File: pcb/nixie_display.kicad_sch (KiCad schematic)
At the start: 12 parts, among them U1 IC_HV5622PG-G, U2 IC_HV5622PG-G

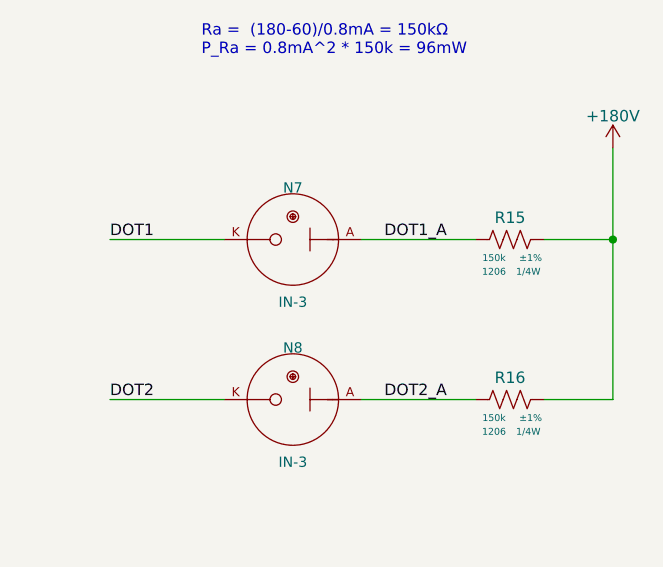
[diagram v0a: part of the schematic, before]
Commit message: Added snubber DNP footprints and named nets on power page.
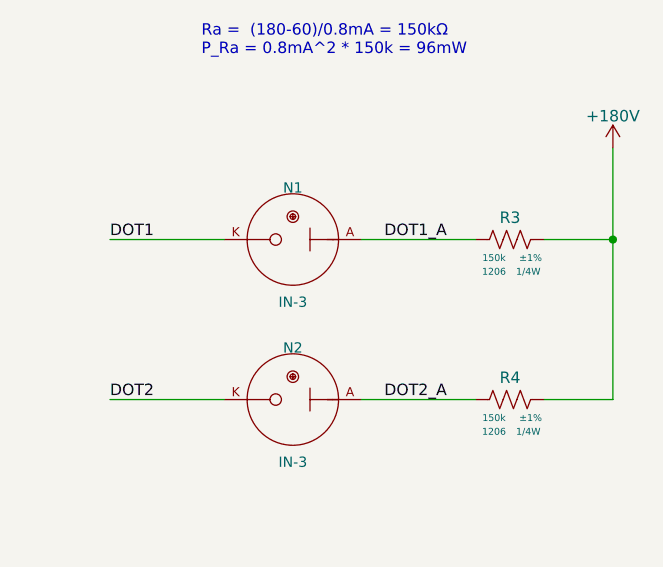
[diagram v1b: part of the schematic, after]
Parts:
- renumbered N7 to N1, N8 to N2, R15 to R3, R16 to R4
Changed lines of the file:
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@@
   (symbol (lib_id "arjun_symbols:RES_150K_1P_1{slash}4W_1206") (at 368.3 124.46 270) (unit 1)
     (in_bom yes) (on_board yes)
-    (property "Reference" "R15" (id 0) (at 364.49 121.285 90)
+    (property "Reference" "R3" (id 0) (at 364.49 121.285 90)
       (effects (font (size 1.27 1.27)) (justify top))
     )
@@
   (symbol (lib_id "arjun_symbols:RES_150K_1P_1{slash}4W_1206") (at 368.3 142.24 270) (unit 1)
     (in_bom yes) (on_board yes)
-    (property "Reference" "R16" (id 0) (at 364.49 139.065 90)
+    (property "Reference" "R4" (id 0) (at 364.49 139.065 90)
       (effects (font (size 1.27 1.27)) (justify top))
     )
@@
   (symbol (lib_id "arjun_symbols:+180V") (at 375.92 114.3 0) (unit 1)
     (in_bom yes) (on_board yes)
-    (property "Reference" "#PWR042" (id 0) (at 375.92 118.11 0)
+    (property "Reference" "#PWR07" (id 0) (at 375.92 118.11 0)
       (effects (font (size 1.27 1.27)) hide)
     )
@@
   (symbol (lib_id "arjun_symbols:IN-3") (at 347.98 142.24 0) (mirror y) (unit 1)
     (in_bom yes) (on_board yes)
-    (property "Reference" "N8" (id 0) (at 340.36 137.16 0)
+    (property "Reference" "N2" (id 0) (at 340.36 137.16 0)
       (effects (font (size 1.143 1.143)) (justify bottom))
     )
@@
   (symbol (lib_id "arjun_symbols:IN-3") (at 347.98 124.46 0) (mirror y) (unit 1)
     (in_bom yes) (on_board yes)
-    (property "Reference" "N7" (id 0) (at 340.36 119.38 0)
+    (property "Reference" "N1" (id 0) (at 340.36 119.38 0)
       (effects (font (size 1.143 1.143)) (justify bottom))
     )

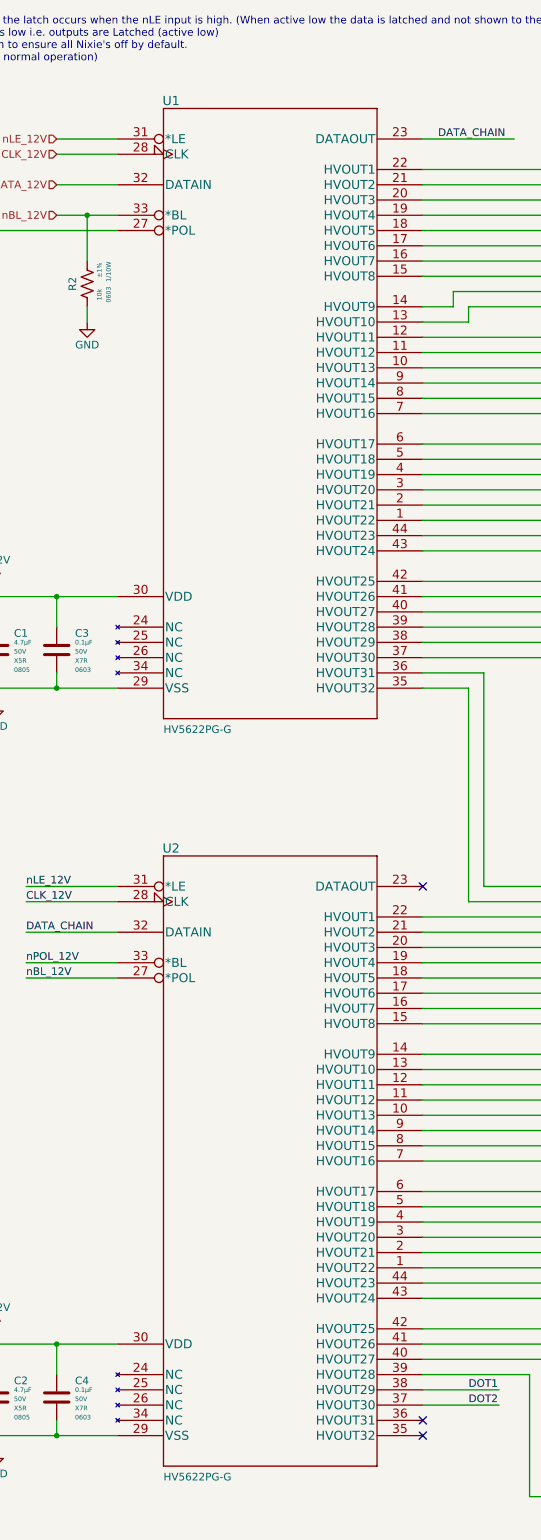
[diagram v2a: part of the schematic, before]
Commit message: Added load switch to input to limit inrush
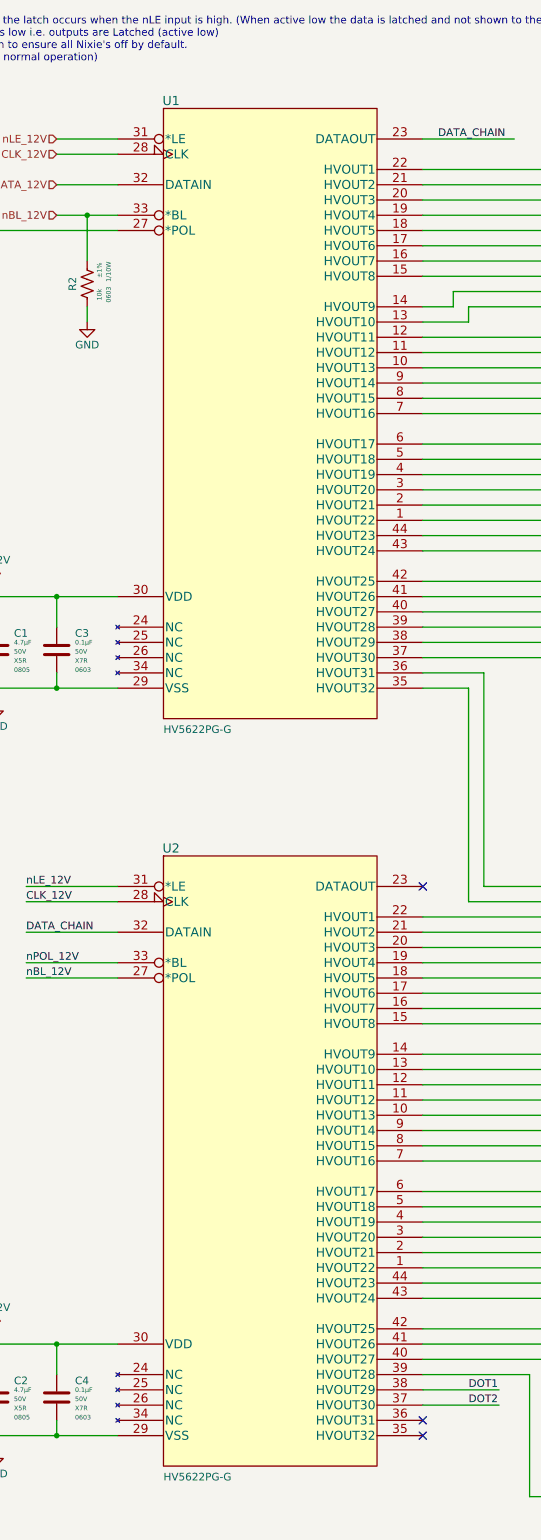
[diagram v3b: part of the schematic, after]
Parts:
- removed U1, U2: IC_HV5622PG-G, arjun_footprints:HV5622PG-G, symbol arjun_symbols:IC_SR_HV5622PG-G
- added U1, U2: IC_SR_MC_HV5622PG-G, arjun_footprints:HV5622PG-G, symbol .arjun:IC_SR_MC_HV5622PG-G
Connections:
- net +12V: now also U1.30 (VDD), U2.30 (VDD)
- net CLK_12V: now also U1.28 (CLK), U2.28 (CLK)
- net DATA_12V: now also U1.32 (DATAIN)
- net DATA_CHAIN: now also U1.23 (DATAOUT), U2.32 (DATAIN)
- net DOT1: now also U2.38 (HVOUT29)
- net DOT2: now also U2.37 (HVOUT30)
- net GND: now also U1.29 (VSS), U2.29 (VSS)
- net H1_0: now also U1.22 (HVOUT1)
- net H1_1: now also U1.21 (HVOUT2)
- net H1_2: now also U1.20 (HVOUT3)
- net H1_3: now also U1.19 (HVOUT4)
- net H1_4: now also U1.18 (HVOUT5)
- net H1_5: now also U1.17 (HVOUT6)
- net H1_6: now also U1.16 (HVOUT7)
- net H1_7: now also U1.15 (HVOUT8)
- net H1_8: now also U1.14 (HVOUT9)
- net H1_9: now also U1.13 (HVOUT10)
- net H2_0: now also U1.12 (HVOUT11)
- net H2_1: now also U1.11 (HVOUT12)
- net H2_2: now also U1.10 (HVOUT13)
- net H2_3: now also U1.9 (HVOUT14)
- net H2_4: now also U1.8 (HVOUT15)
- net H2_5: now also U1.7 (HVOUT16)
- net H2_6: now also U1.6 (HVOUT17)
- net H2_7: now also U1.5 (HVOUT18)
- net H2_8: now also U1.4 (HVOUT19)
- net H2_9: now also U1.3 (HVOUT20)
- net M1_0: now also U1.2 (HVOUT21)
- net M1_1: now also U1.1 (HVOUT22)
- net M1_2: now also U1.44 (HVOUT23)
- net M1_3: now also U1.43 (HVOUT24)
- net M1_4: now also U1.42 (HVOUT25)
- net M1_5: now also U1.41 (HVOUT26)
- net M1_6: now also U1.40 (HVOUT27)
- net M1_7: now also U1.39 (HVOUT28)
- net M1_8: now also U1.38 (HVOUT29)
- net M1_9: now also U1.37 (HVOUT30)
- net M2_0: now also U1.36 (HVOUT31)
- net M2_1: now also U1.35 (HVOUT32)
- net M2_2: now also U2.22 (HVOUT1)
- net M2_3: now also U2.21 (HVOUT2)
- net M2_4: now also U2.20 (HVOUT3)
- net M2_5: now also U2.19 (HVOUT4)
- net M2_6: now also U2.18 (HVOUT5)
- net M2_7: now also U2.17 (HVOUT6)
- net M2_8: now also U2.16 (HVOUT7)
- net M2_9: now also U2.15 (HVOUT8)
- net S1_0: now also U2.14 (HVOUT9)
- net S1_1: now also U2.13 (HVOUT10)
- net S1_2: now also U2.12 (HVOUT11)
- net S1_3: now also U2.11 (HVOUT12)
- net S1_4: now also U2.10 (HVOUT13)
- net S1_5: now also U2.9 (HVOUT14)
- net S1_6: now also U2.8 (HVOUT15)
- net S1_7: now also U2.7 (HVOUT16)
- net S1_8: now also U2.6 (HVOUT17)
- net S1_9: now also U2.5 (HVOUT18)
- net S2_0: now also U2.4 (HVOUT19)
- net S2_1: now also U2.3 (HVOUT20)
- net S2_2: now also U2.2 (HVOUT21)
- net S2_3: now also U2.1 (HVOUT22)
- net S2_4: now also U2.44 (HVOUT23)
- net S2_5: now also U2.43 (HVOUT24)
- net S2_6: now also U2.42 (HVOUT25)
- net S2_7: now also U2.41 (HVOUT26)
- net S2_8: now also U2.40 (HVOUT27)
- net S2_9: now also U2.39 (HVOUT28)
- net nBL_12V: now also U1.33 (*BL), U2.27 (*POL)
- net nLE_12V: now also U1.31 (*LE), U2.31 (*LE)
- net nPOL_12V: now also U1.27 (*POL), U2.33 (*BL)

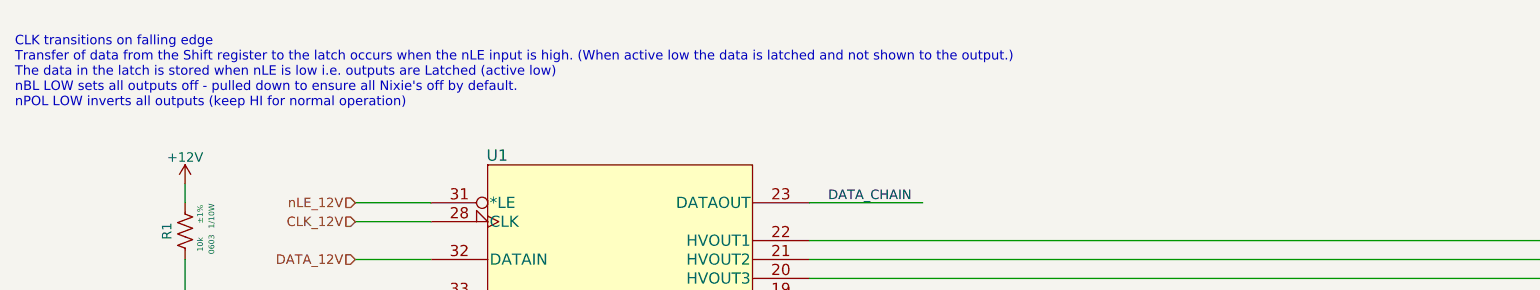
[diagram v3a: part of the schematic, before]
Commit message: Added ESD protection to 5V input, leds, hw rev pins, and test points.
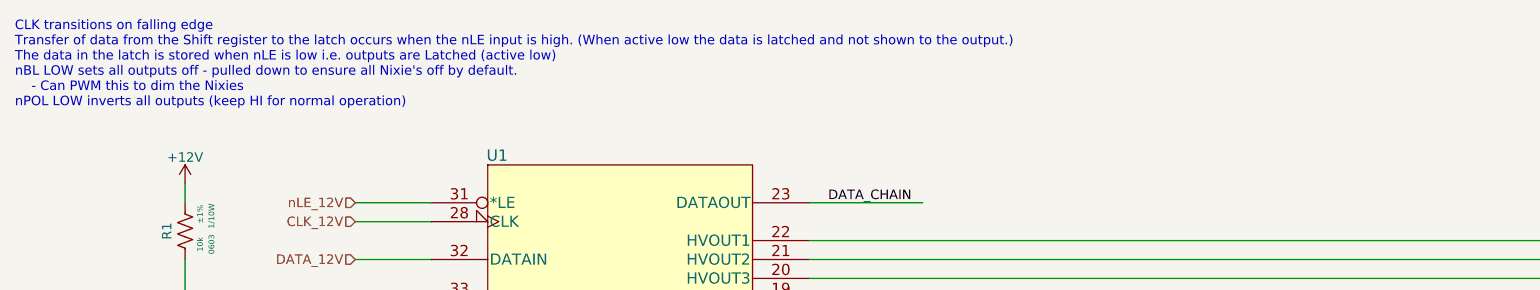
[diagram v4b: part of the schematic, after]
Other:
- note added: "CLK transitions on falling edge Transfer of data from the Shift register to the latch occurs when the nLE input is high. (When active low the data is latched and not shown to the output.) The data in the latch is stored when nLE is low i.e. outputs are Latched (active low) nBL LOW sets all outputs off - pulled down to ensure all Nixie's off by default. - Can PWM this to dim the Nixies nPOL LOW in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"
- note removed: "CLK transitions on falling edge Transfer of data from the Shift register to the latch occurs when the nLE input is high. (When active low the data is latched and not shown to the output.) The data in the latch is stored when nLE is low i.e. outputs are Latched (active low) nBL LOW sets all outputs off - pulled down to ensure all Nixie's off by default. nPOL LOW inverts all outputs (keep HI for no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"
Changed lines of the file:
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@@
     (stroke (width 0) (type default) (color 0 0 0 0))
   )
-  (text "CLK transitions on falling edge\nTransfer of data from the Shift register to the latch occurs when the nLE input is high. (When active low the data is latched and not shown to the output.)\nThe data in the latch is stored when nLE is low i.e. outputs are Latched (active low)\nnBL LOW sets all outputs off - pulled down to ensure all Nixie's off by default.\nnPOL LOW inverts all outputs (keep HI for normal operation)\n"
+  (text "CLK transitions on falling edge\nTransfer of data from the Shift register to the latch occurs when the nLE input is high. (When active low the data is latched and not shown to the output.)\nThe data in the latch is stored when nLE is low i.e. outputs are Latched (active low)\nnBL LOW sets all outputs off - pulled down to ensure all Nixie's off by default.\n	- Can PWM this to dim the Nixies\nnPOL LOW inverts all outputs (keep HI for normal operation)\n"
     (at 15.24 25.4 0)
     (effects (font (size 1.27 1.27)) (justify left bottom))

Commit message: Started layout!! 180V boost mostly laid out
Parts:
- R1, R2: symbol arjun_symbols:RES_10K_1P_1/10W_0603 -> arjun_symbols:RES_10K_1P_1/10W_0603
- R3, R4: symbol arjun_symbols:RES_150K_1P_1/4W_1206 -> arjun_symbols:RES_150K_1P_1/4W_1206

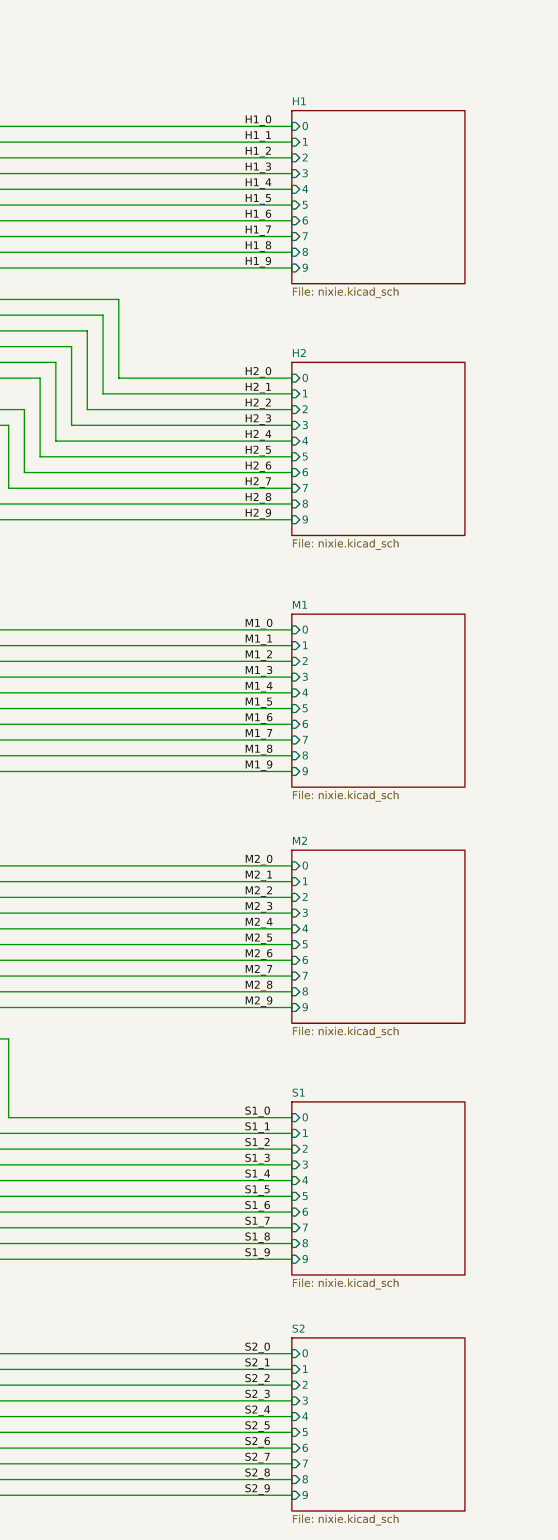
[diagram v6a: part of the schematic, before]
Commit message: Making progress on nixie tube signal routing
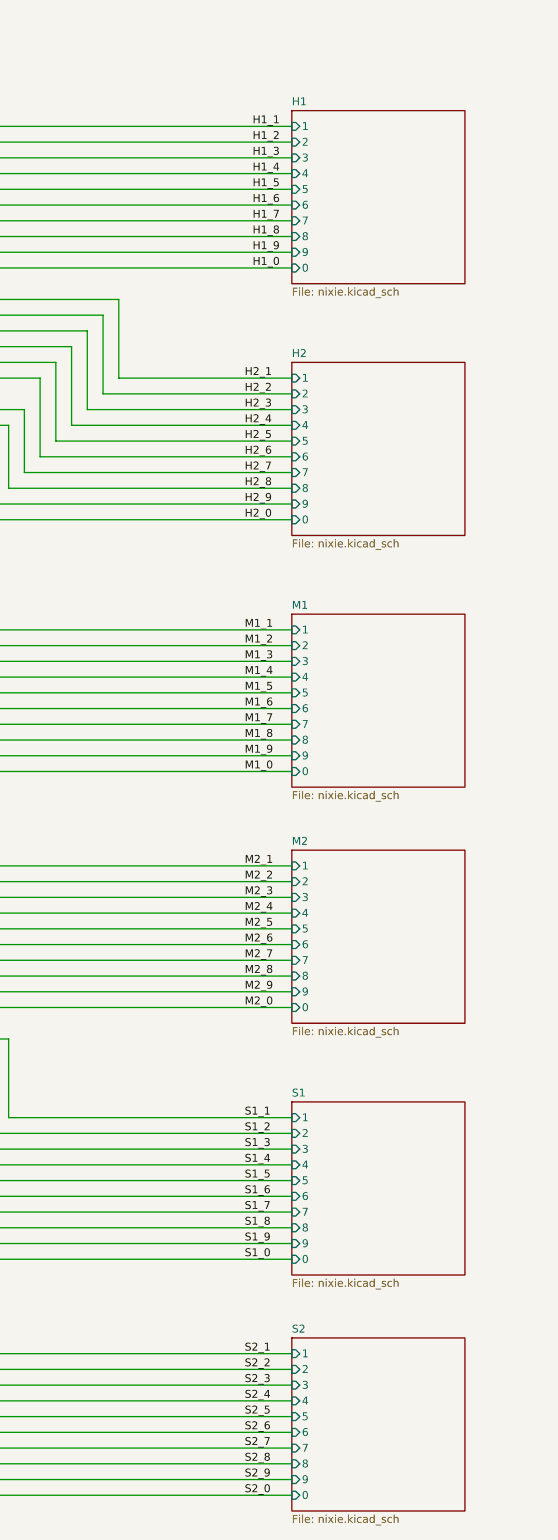
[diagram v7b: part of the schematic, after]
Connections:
- net H1_0: now also U1.13 (HVOUT10); no longer U1.22 (HVOUT1)
- net H1_1: now also U1.22 (HVOUT1); no longer U1.21 (HVOUT2)
- net H1_2: now also U1.21 (HVOUT2); no longer U1.20 (HVOUT3)
- net H1_3: now also U1.20 (HVOUT3); no longer U1.19 (HVOUT4)
- net H1_4: now also U1.19 (HVOUT4); no longer U1.18 (HVOUT5)
- net H1_5: now also U1.18 (HVOUT5); no longer U1.17 (HVOUT6)
- net H1_6: now also U1.17 (HVOUT6); no longer U1.16 (HVOUT7)
- net H1_7: now also U1.16 (HVOUT7); no longer U1.15 (HVOUT8)
- net H1_8: now also U1.15 (HVOUT8); no longer U1.14 (HVOUT9)
- net H1_9: now also U1.14 (HVOUT9); no longer U1.13 (HVOUT10)
- net H2_0: now also U1.3 (HVOUT20); no longer U1.12 (HVOUT11)
- net H2_1: now also U1.12 (HVOUT11); no longer U1.11 (HVOUT12)
- net H2_2: now also U1.11 (HVOUT12); no longer U1.10 (HVOUT13)
- net H2_3: now also U1.10 (HVOUT13); no longer U1.9 (HVOUT14)
- net H2_4: now also U1.9 (HVOUT14); no longer U1.8 (HVOUT15)
- net H2_5: now also U1.8 (HVOUT15); no longer U1.7 (HVOUT16)
- net H2_6: now also U1.7 (HVOUT16); no longer U1.6 (HVOUT17)
- net H2_7: now also U1.6 (HVOUT17); no longer U1.5 (HVOUT18)
- net H2_8: now also U1.5 (HVOUT18); no longer U1.4 (HVOUT19)
- net H2_9: now also U1.4 (HVOUT19); no longer U1.3 (HVOUT20)
- net M1_0: now also U1.37 (HVOUT30); no longer U1.2 (HVOUT21)
- net M1_1: now also U1.2 (HVOUT21); no longer U1.1 (HVOUT22)
- net M1_2: now also U1.1 (HVOUT22); no longer U1.44 (HVOUT23)
- net M1_3: now also U1.44 (HVOUT23); no longer U1.43 (HVOUT24)
- net M1_4: now also U1.43 (HVOUT24); no longer U1.42 (HVOUT25)
- net M1_5: now also U1.42 (HVOUT25); no longer U1.41 (HVOUT26)
- net M1_6: now also U1.41 (HVOUT26); no longer U1.40 (HVOUT27)
- net M1_7: now also U1.40 (HVOUT27); no longer U1.39 (HVOUT28)
- net M1_8: now also U1.39 (HVOUT28); no longer U1.38 (HVOUT29)
- net M1_9: now also U1.38 (HVOUT29); no longer U1.37 (HVOUT30)
- net M2_0: now also U2.15 (HVOUT8); no longer U1.36 (HVOUT31)
- net M2_1: now also U1.36 (HVOUT31); no longer U1.35 (HVOUT32)
- net M2_2: now also U1.35 (HVOUT32); no longer U2.22 (HVOUT1)
- net M2_3: now also U2.22 (HVOUT1); no longer U2.21 (HVOUT2)
- net M2_4: now also U2.21 (HVOUT2); no longer U2.20 (HVOUT3)
- net M2_5: now also U2.20 (HVOUT3); no longer U2.19 (HVOUT4)
- net M2_6: now also U2.19 (HVOUT4); no longer U2.18 (HVOUT5)
- net M2_7: now also U2.18 (HVOUT5); no longer U2.17 (HVOUT6)
- net M2_8: now also U2.17 (HVOUT6); no longer U2.16 (HVOUT7)
- net M2_9: now also U2.16 (HVOUT7); no longer U2.15 (HVOUT8)
- net S1_0: now also U2.5 (HVOUT18); no longer U2.14 (HVOUT9)
- net S1_1: now also U2.14 (HVOUT9); no longer U2.13 (HVOUT10)
- net S1_2: now also U2.13 (HVOUT10); no longer U2.12 (HVOUT11)
- net S1_3: now also U2.12 (HVOUT11); no longer U2.11 (HVOUT12)
- net S1_4: now also U2.11 (HVOUT12); no longer U2.10 (HVOUT13)
- net S1_5: now also U2.10 (HVOUT13); no longer U2.9 (HVOUT14)
- net S1_6: now also U2.9 (HVOUT14); no longer U2.8 (HVOUT15)
- net S1_7: now also U2.8 (HVOUT15); no longer U2.7 (HVOUT16)
- net S1_8: now also U2.7 (HVOUT16); no longer U2.6 (HVOUT17)
- net S1_9: now also U2.6 (HVOUT17); no longer U2.5 (HVOUT18)
- net S2_0: now also U2.39 (HVOUT28); no longer U2.4 (HVOUT19)
- net S2_1: now also U2.4 (HVOUT19); no longer U2.3 (HVOUT20)
- net S2_2: now also U2.3 (HVOUT20); no longer U2.2 (HVOUT21)
- net S2_3: now also U2.2 (HVOUT21); no longer U2.1 (HVOUT22)
- net S2_4: now also U2.1 (HVOUT22); no longer U2.44 (HVOUT23)
- net S2_5: now also U2.44 (HVOUT23); no longer U2.43 (HVOUT24)
- net S2_6: now also U2.43 (HVOUT24); no longer U2.42 (HVOUT25)
- net S2_7: now also U2.42 (HVOUT25); no longer U2.41 (HVOUT26)
- net S2_8: now also U2.41 (HVOUT26); no longer U2.40 (HVOUT27)
- net S2_9: now also U2.40 (HVOUT27); no longer U2.39 (HVOUT28)
